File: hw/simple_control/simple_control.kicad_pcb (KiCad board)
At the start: 4 copper layers, 80 x 100 mm, 105 parts, among them J101 Screw_Terminal_01x02, J102 Jack-DC, J103 Screw_Terminal_01x03, J104 Screw_Terminal_01x03, J1301 Micro_SD_Card, J1401 Conn_02x05_Odd_Even, J601 Conn_01x04, J602 Raspberry_Pi_0_2_3, J603 Conn_01x03, Q1001 BC817, Q201 AOSP21357, Q701 BC817, Q801 BC817, Q901 BC817, SW1801 SW_Push, SW1901 SW_Push, SW2001 SW_Push, SW2101 SW_Push, SW602 SW_Push, U1101 CAT24C256, U1501 4050, U301 SN74AHCT125D, U601 PicoW

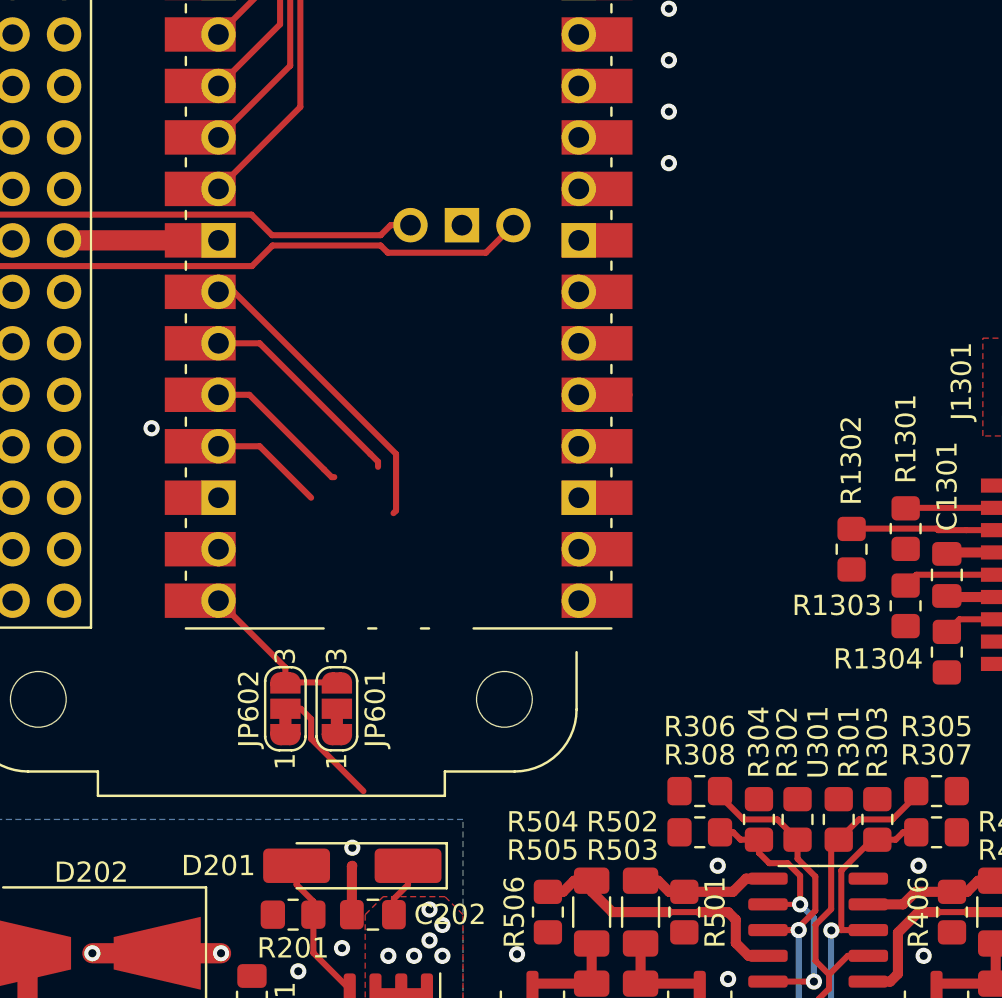
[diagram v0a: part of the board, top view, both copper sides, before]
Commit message: chore(hw): layout LED EN and DATA
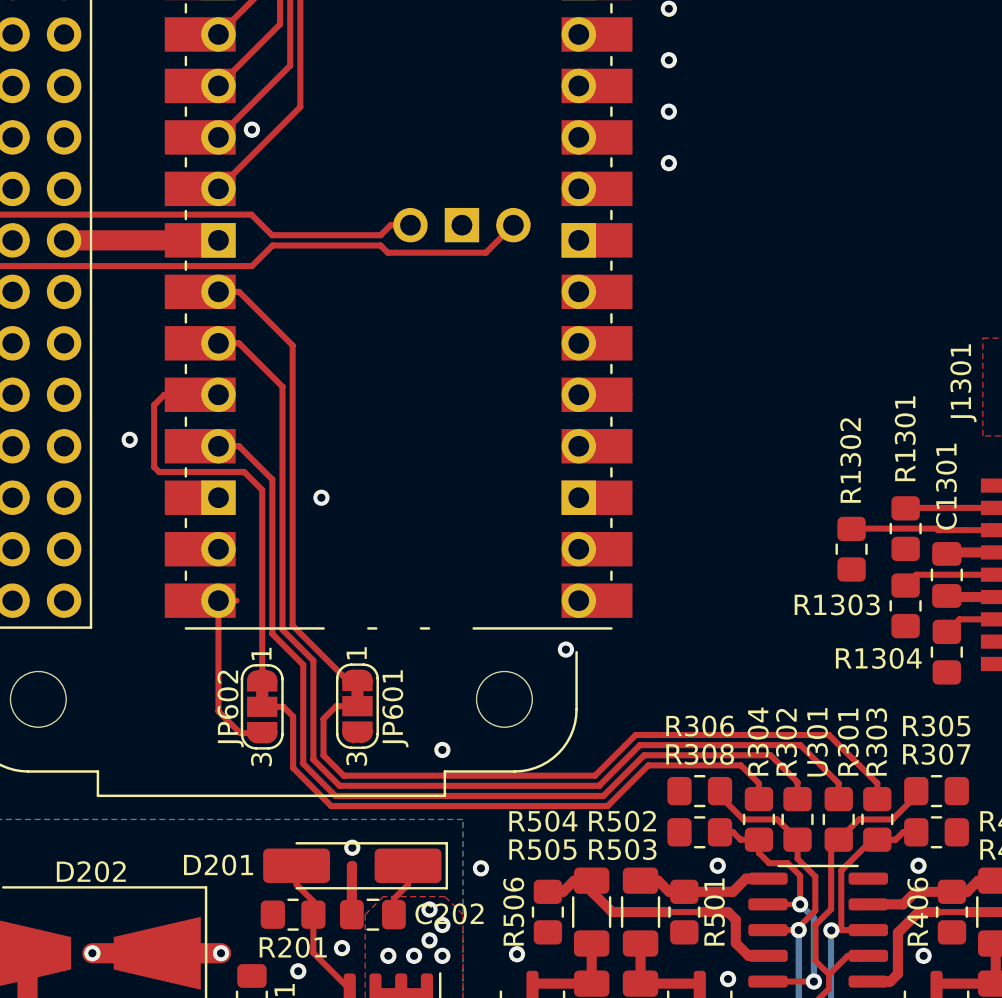
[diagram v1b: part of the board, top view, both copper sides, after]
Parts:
- moved JP602 1.15 mm to (127.3, 108.6), turned to -90 degrees
- moved JP601 1.02 mm to (132.0, 108.6), turned to -90 degrees
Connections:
- U601 pad 19: /CPU/BUTTON3 -> unconnected-(U601-GPIO14-Pad19)
- U601 pad 31: unconnected-(U601-GPIO26_ADC0-Pad31) -> /CPU/BUTTON3
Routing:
- net /LED_DATA_~{EN}0: track 44.3 -> 85.8 mm
- net /LED_DATA_~{EN}1: track 16.8 -> 56.5 mm
- net /LED_DATA0: track 0.00 -> 34.1 mm
- net /CPU/BUTTON3: track 8.67 -> 41.7 mm, vias 0 -> 1
- net /LED_DATA1: track 6.13 -> 30.0 mm
- net /CPU/PRIM_LED_DATA1: track 16.1 -> 30.3 mm
- net /CPU/PRIM_LED_DATA0: track 27.3 -> 35.2 mm
- net /CPU/ALT_LED_DATA: track 19.2 -> 20.2 mm
- net /CPU/STAT_LED2: track 92.2 -> 93.0 mm
- net /CPU/BUTTON2: track 35.6 -> 36.1 mm
- net GND: vias 26 -> 30

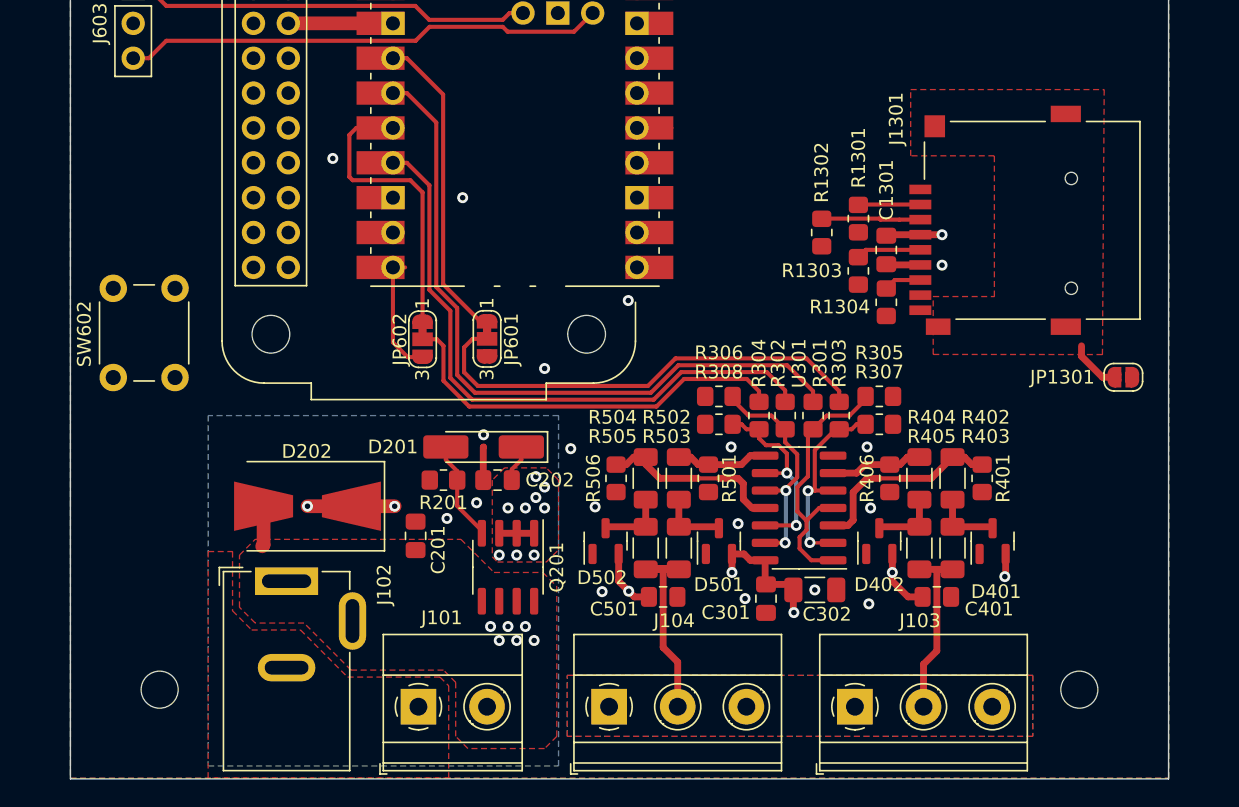
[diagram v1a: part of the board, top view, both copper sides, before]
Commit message: chore(hw): layout sd card signals
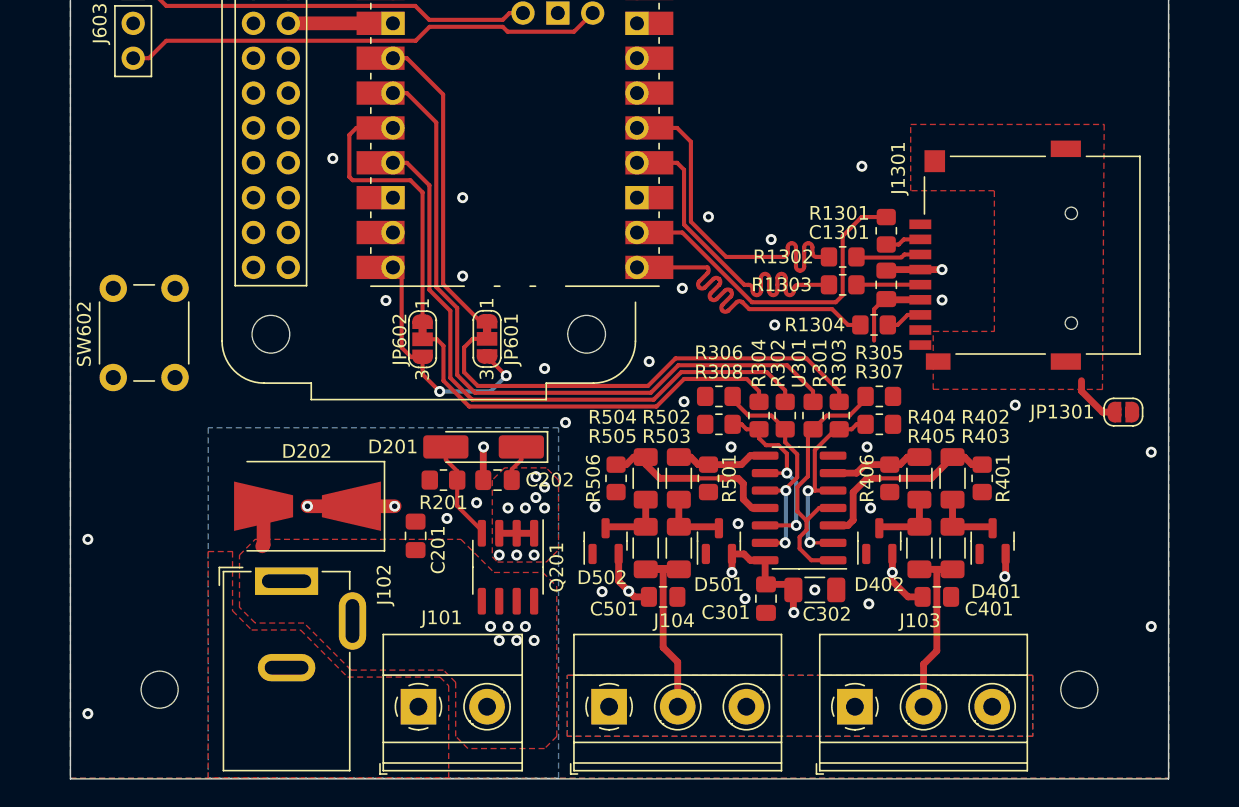
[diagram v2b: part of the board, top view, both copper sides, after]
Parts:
- moved J1301 2.54 mm to (174.5, 102.5)
- moved C1301 2.54 mm to (161.0, 104.6)
- moved JP1301 2.54 mm to (178.3, 113.9)
- moved R1302 2.34 mm to (157.9, 102.6), turned to 0 degrees
- moved R1301 2.22 mm to (161.0, 100.7), turned to -90 degrees
- moved R1304 1.88 mm to (160.1, 107.6), turned to 0 degrees
- moved R1303 1.53 mm to (157.9, 104.6), turned to 0 degrees
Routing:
- net /CPU/SPI_FLASH_CLK: track 48.4 -> 74.4 mm
- net /CPU/SPI_FLASH_~{CS}: track 58.0 -> 83.4 mm
- net /CPU/SPI_FLASH_MISO: track 61.0 -> 86.0 mm
- net /CPU/SPI_FLASH_MOSI: track 56.0 -> 79.6 mm
- net /CPU/ALT_LED_DATA: track 20.2 -> 29.4 mm, vias 0 -> 2
- net GND: track 38.8 -> 42.3 mm, vias 30 -> 43
- net Net-(J1301-CMD): track 7.22 -> 4.70 mm
- net Net-(J1301-DAT3/CD): track 4.52 -> 2.64 mm

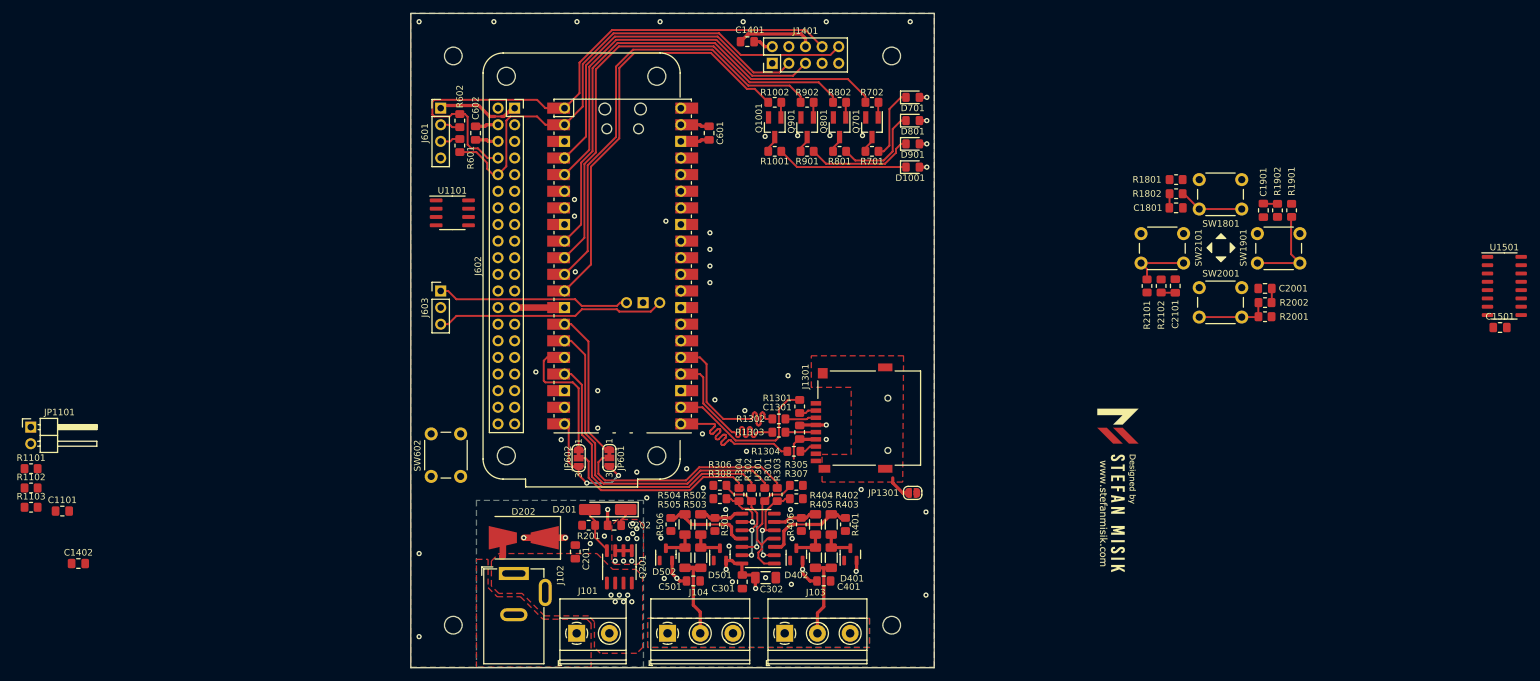
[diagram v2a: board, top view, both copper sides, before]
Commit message: chore(hw): add missing RTC module connection
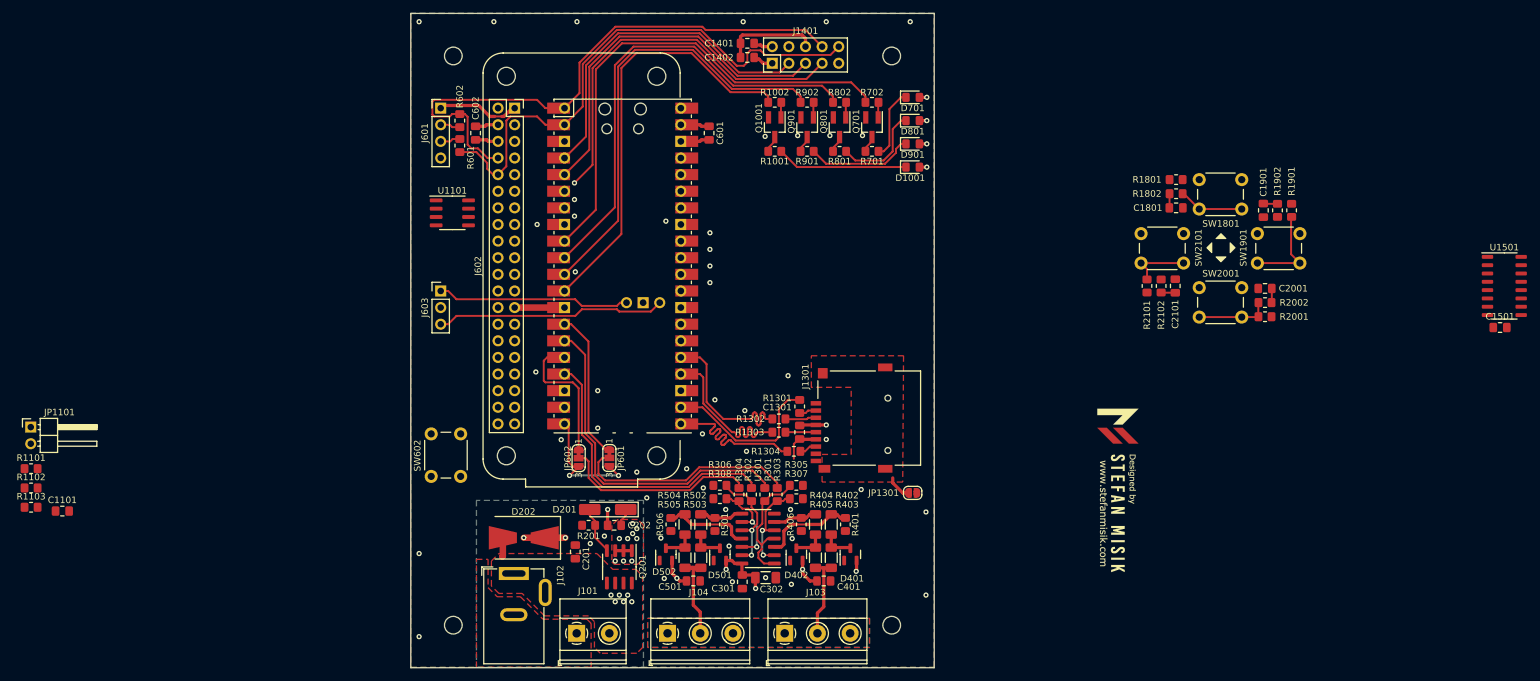
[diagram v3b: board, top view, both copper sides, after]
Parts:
- moved C1402 128.2 mm to (153.0, 47.4)
- moved C1401 0.25 mm to (153.0, 45.2)
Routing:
- net /CPU/RTC_GPIO: track 28.6 -> 87.6 mm, vias 0 -> 1
- net /CPU/TERM_RXD: track 79.7 -> 82.8 mm
- net +3.3V: track 56.8 -> 59.8 mm
- net GND: track 42.3 -> 45.2 mm
- net /CPU/STAT_LED1: track 83.7 -> 82.4 mm
- net /CPU/ALT_LED_DATA: track 29.4 -> 30.5 mm

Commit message: chore(hw): layout ID EEPROM
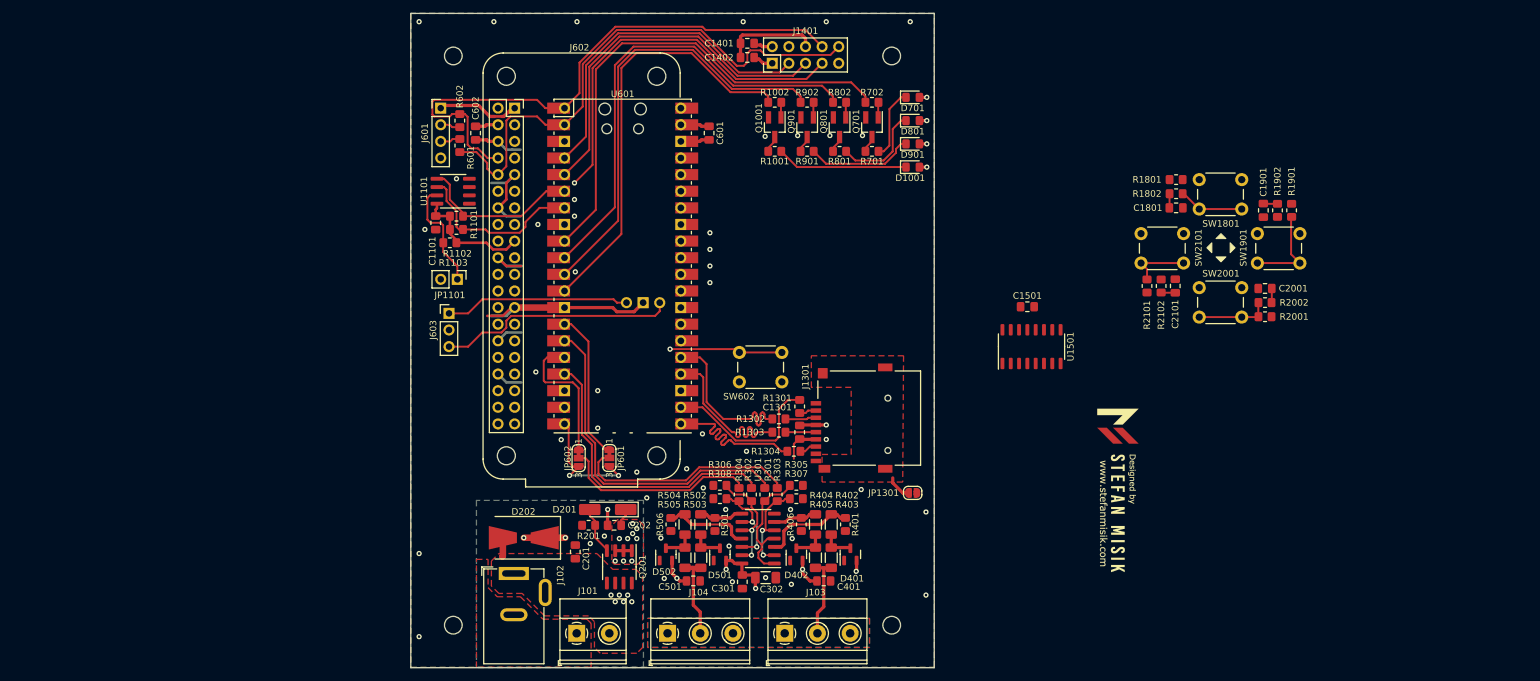
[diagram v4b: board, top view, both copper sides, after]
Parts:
- JP1101: footprint Connector_PinHeader_2.54mm:PinHeader_1x02_P2.54mm_Horizontal -> Connector_PinHeader_2.54mm:PinHeader_1x02_P2.54mm_Vertical
- moved R1102 76.1 mm to (108.6, 73.7)
- moved R1103 75.7 mm to (107.6, 75.7), turned to 180 degrees
- moved R1101 75.6 mm to (108.6, 71.6)
- moved U1501 72.9 mm to (196.5, 91.6), turned to 90 degrees
- moved C1501 72.3 mm to (195.8, 85.5)
- moved C1101 72.1 mm to (105.4, 72.6), turned to -90 degrees
- moved JP1101 69.0 mm to (108.7, 81.3), turned to -90 degrees
- moved SW602 44.4 mm to (151.8, 92.5), turned to 0 degrees
- moved J603 3.66 mm to (107.4, 86.5)
- moved U1101 3.30 mm to (108.1, 67.8), turned to 180 degrees
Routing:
- net GND: track 45.2 -> 101.6 mm, vias 43 -> 42
- net (no net): track 36.2 -> 0.00 mm, vias 1 -> 0
- net Net-(U601-RUN): track 0.00 -> 30.0 mm, vias 0 -> 1
- net /CPU/ID_SCL: track 26.6 -> 53.4 mm
- net /CPU/ID_SDA: track 25.2 -> 50.3 mm
- net +3.3V: track 59.8 -> 78.9 mm
- net Net-(JP1101-A): track 0.00 -> 16.9 mm
- net Net-(J603-Pin_1): track 29.5 -> 28.2 mm
- net Net-(J603-Pin_3): track 35.1 -> 36.4 mm

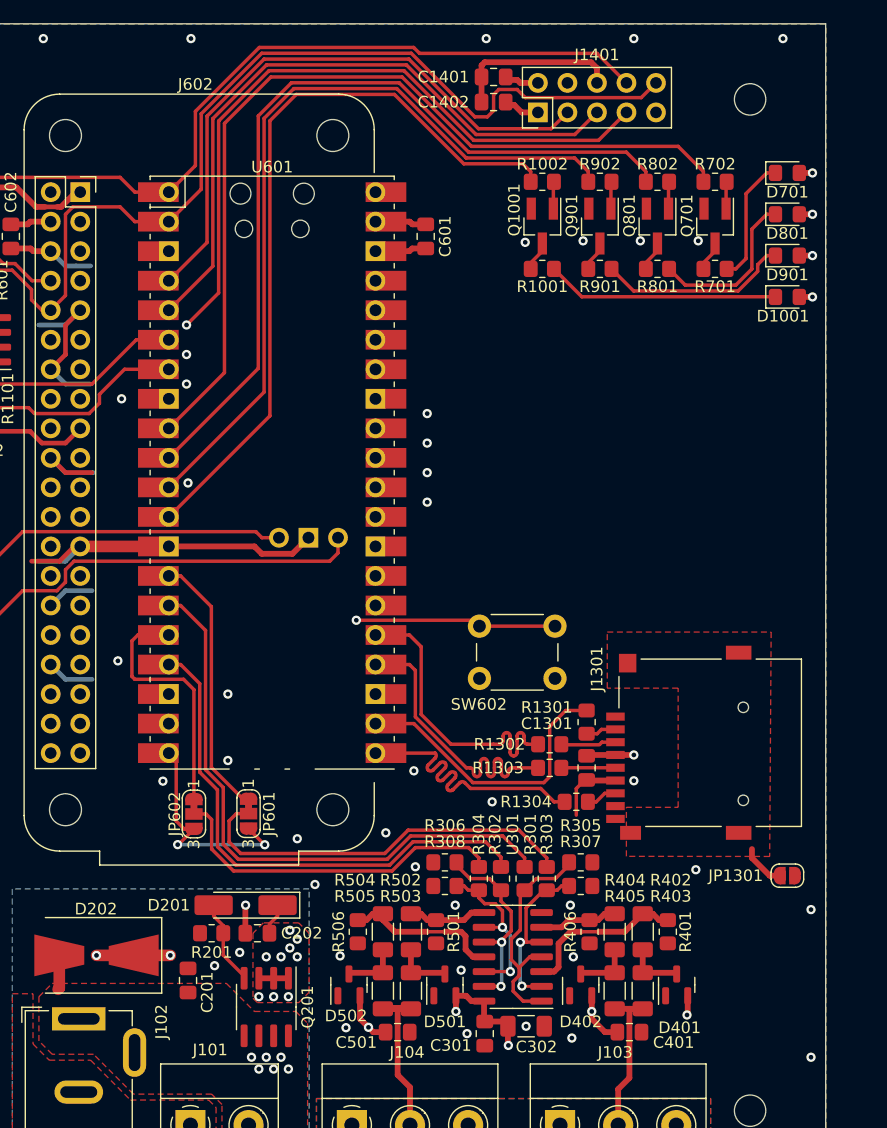
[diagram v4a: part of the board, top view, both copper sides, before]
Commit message: chore(hw): fix DRC violations
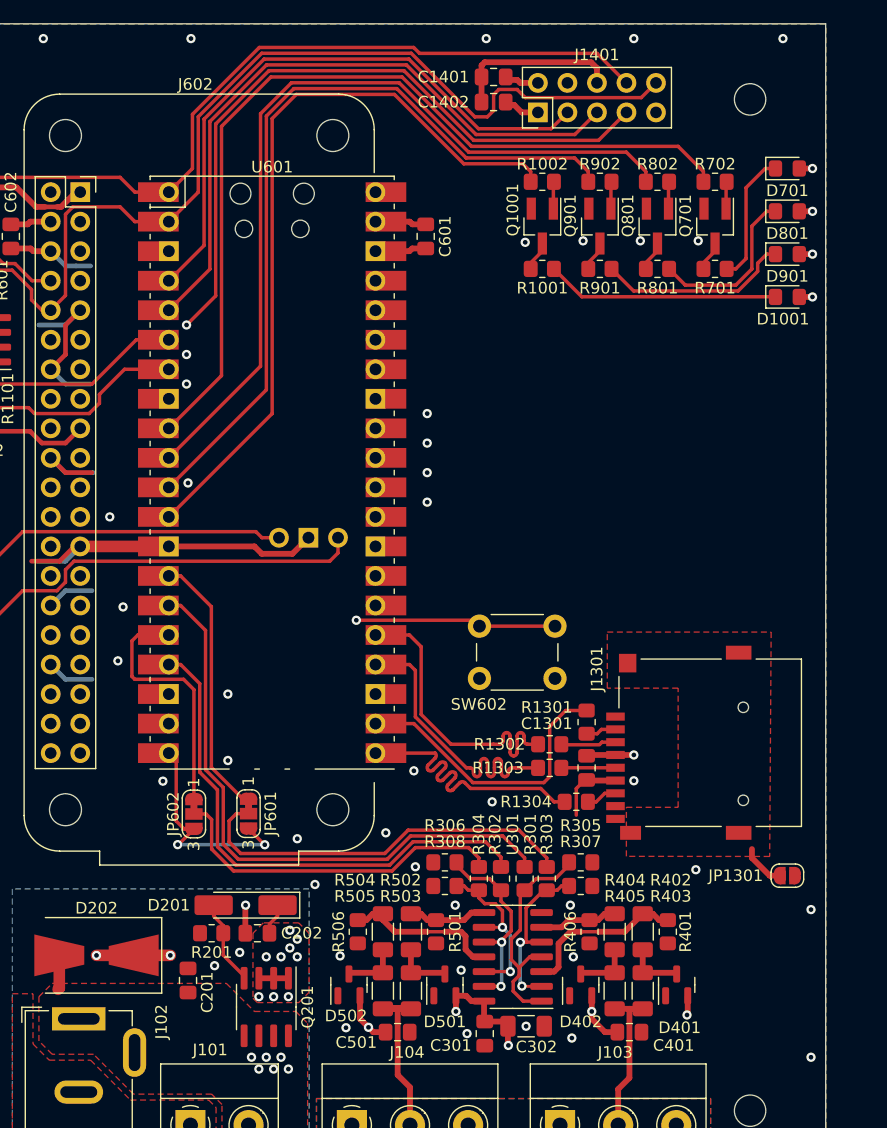
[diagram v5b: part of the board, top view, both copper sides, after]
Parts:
- moved D701 0.38 mm to (178.3, 53.1)
- moved D801 0.25 mm to (178.3, 56.8)
- moved D901 0.13 mm to (178.3, 60.5)
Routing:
- net GND: vias 42 -> 43
